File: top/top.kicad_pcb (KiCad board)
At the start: 2 copper layers, 28.3 x 40 mm, 26 parts, among them P1 CONN_10, P2 CONN_5, U1 IQS572, U4 ESD

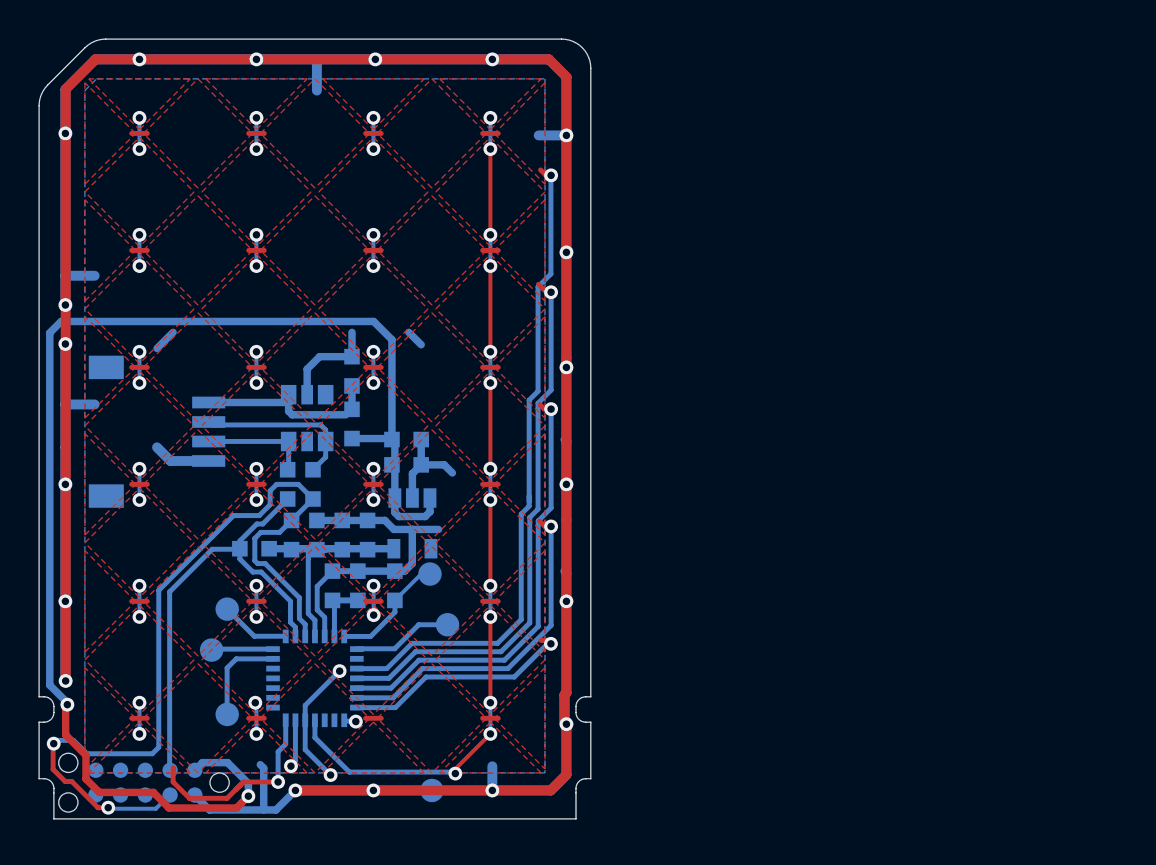
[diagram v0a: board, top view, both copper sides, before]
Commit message: Edit ESD GND ring.
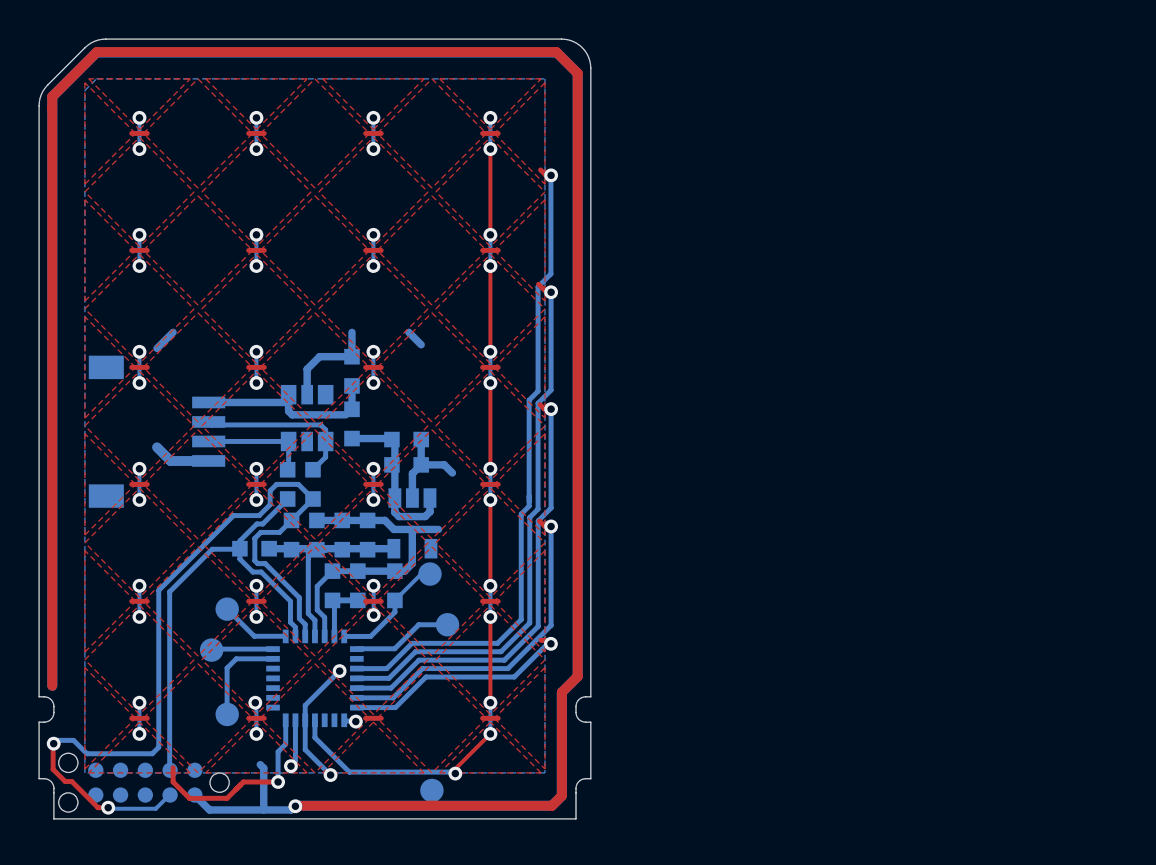
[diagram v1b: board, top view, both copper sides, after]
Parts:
- removed G***: LOGO, ugl:UHK_Logo_12x3.4_mm
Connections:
- P1 pad 2: +5V -> /VCC_BOTTOM
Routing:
- net +5V: track 68.7 -> 8.57 mm, vias 2 -> 0
- net GND: track 259.6 -> 259.0 mm, vias 19 -> 1

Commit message: New diamond pattern.
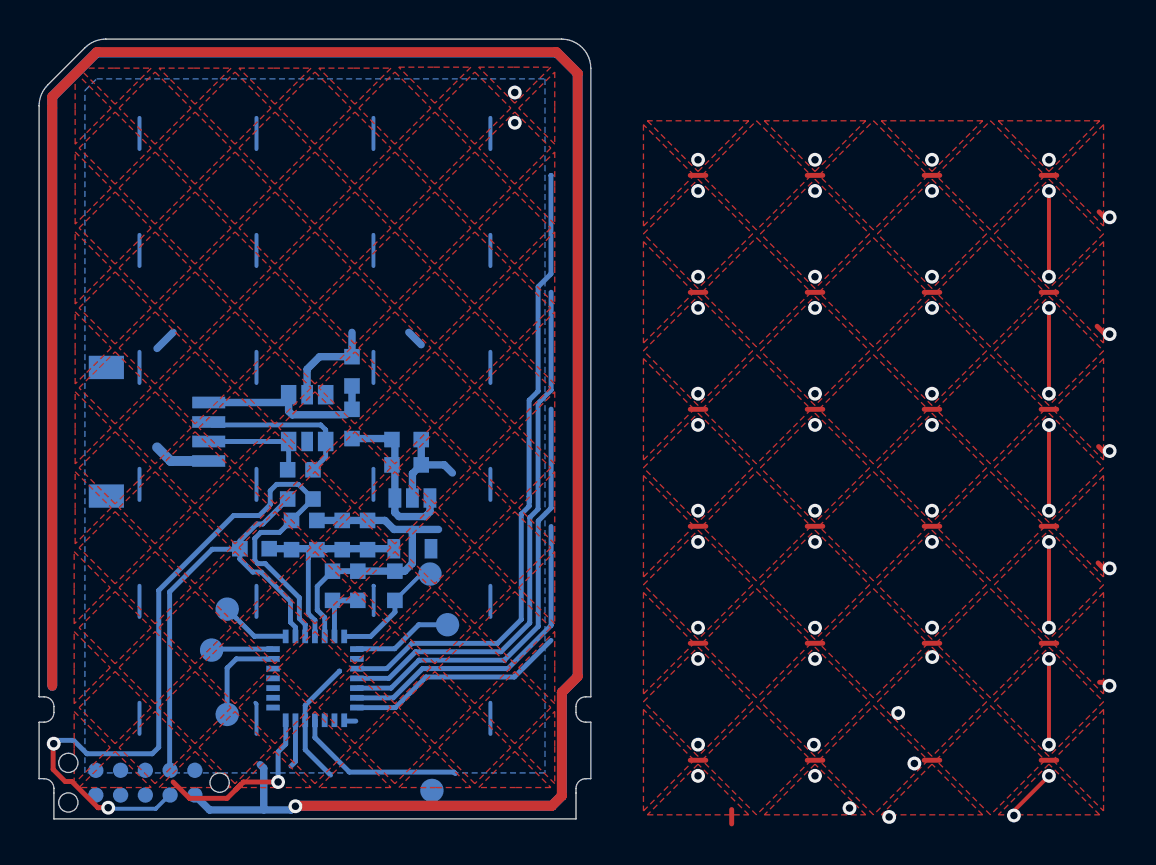
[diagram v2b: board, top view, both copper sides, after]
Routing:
- net (no net): vias 0 -> 2
- added copper zone on F.Cu, net (none)

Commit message: Wiring new pattern.
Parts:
- removed TP_NRST1: NRST, ugl:Test_Point
- removed TP_PGM1: PGM, ugl:Test_Point
- removed TP_RDY1: RDY, ugl:Test_Point
- moved TP_GND1 20.0 mm to (192.5, 151.5)
- moved C2 7.08 mm to (205.7, 135.0), turned to 90 degrees
- moved C8 5.32 mm to (206.9, 135.0), turned to 90 degrees
- moved VR1 5.08 mm to (209.8, 138.3)
- moved C7 5.00 mm to (202.6, 135.3)
- moved R1 4.65 mm to (208.6, 141.7), turned to 90 degrees
- moved C6 4.48 mm to (211.0, 141.7), turned to 90 degrees
- moved FB2 4.46 mm to (204.5, 135.0), turned to 90 degrees
- moved R2 4.24 mm to (205.7, 141.7), turned to 90 degrees
- moved TP_POUT1 3.47 mm to (202.9, 152.2)
- moved TP_TOUT1 2.79 mm to (201.9, 150.4)
- moved C12 2.61 mm to (209.8, 141.7), turned to 90 degrees
- moved C5 2.20 mm to (204.1, 145.3)
- moved U1 2.17 mm to (207.8, 150.7), turned to 315 degrees
- moved P2 1.90 mm to (196.2, 138.6)
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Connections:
- net Net-(U1-Pad22) renamed /TX4
- net Net-(U1-Pad23) renamed /TX5
- net Net-(U1-Pad24) renamed /TX6
- net Net-(U1-Pad25) renamed /TX7
- net Net-(U1-Pad26) renamed /TX8
- P1 pad 10: Net-(P1-Pad10) -> /PGM
- P1 pad 8: Net-(P1-Pad8) -> /RDY
- P1 pad 9: Net-(P1-Pad9) -> /NRST
- U1 pad 27: Net-(TP_PGM1-Pad1) -> /PGM
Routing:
- net (no net): track 0.00 -> 41.6 mm, vias 2 -> 0
- net /RX5: track 3.81 -> 40.5 mm, vias 1 -> 10
- net /RX4: track 15.2 -> 36.1 mm, vias 1 -> 11
- net /TX1: track 14.5 -> 34.5 mm, vias 12 -> 1
- net /RX3: track 20.5 -> 40.2 mm, vias 1 -> 10
- net /TX2: track 12.1 -> 31.4 mm, vias 13 -> 1
- net GND: track 259.0 -> 242.7 mm, vias 1 -> 7
- net /VCC_BOTTOM: track 9.56 -> 25.1 mm
- net /SCL: track 43.2 -> 28.4 mm
- net +3V3: track 11.6 -> 25.7 mm
- net /RX2: track 25.9 -> 34.5 mm, vias 1 -> 10
- net /TX3: track 20.1 -> 28.3 mm, vias 13 -> 1
- net /NRST: track 6.09 -> 0.00 mm
- net /RDY: track 5.14 -> 0.00 mm
- net /TX0: track 43.2 -> 38.3 mm, vias 13 -> 1
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- added copper zone on F.Cu, net /TX4
- added copper zone on F.Cu, net /TX5
- added copper zone on F.Cu, net /TX6
- added copper zone on F.Cu, net /TX7
- added copper zone on F.Cu, net /TX8
- added copper zone on In1.Cu, net GND
- removed copper zone on F.Cu, net (none)
- removed copper zone on B.Cu, net GND
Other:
- copper layers 2 -> 4

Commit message: First final modified board.
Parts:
- moved C1 17.7 mm to (193.3, 153.4), turned to 90 degrees
- moved TP_TOUT1 1.08 mm to (201.5, 151.4)
- moved C12 0.50 mm to (210.3, 141.7)
- moved C6 0.50 mm to (211.5, 141.7)
- moved TP_GND1 0.22 mm to (192.3, 151.4)
- moved C3 0.20 mm to (206.9, 145.5)
- moved C4 0.20 mm to (205.7, 145.5)
- moved C5 0.20 mm to (204.1, 145.5)
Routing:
- net (no net): track 41.6 -> 0.00 mm
- net /TX4: track 0.00 -> 30.1 mm, vias 0 -> 1
- net /NRST: track 0.00 -> 27.5 mm, vias 0 -> 2
- net /TX5: track 0.00 -> 26.4 mm, vias 0 -> 1
- net /RDY: track 0.00 -> 26.0 mm, vias 0 -> 2
- net /TX6: track 0.00 -> 25.0 mm, vias 0 -> 1
- net /RX0: track 34.5 -> 52.1 mm, vias 10 -> 11
- net /PGM: track 0.00 -> 13.8 mm, vias 0 -> 2
- net /RX1: track 34.5 -> 46.4 mm, vias 9 -> 11
- net /RX2: track 34.5 -> 43.4 mm, vias 10 -> 11
- net /TX8: track 3.44 -> 8.24 mm
- net /TX7: track 1.36 -> 6.16 mm
- net /TX1: track 34.5 -> 37.9 mm
- net /TX2: track 31.4 -> 34.8 mm
- net /TX3: track 28.3 -> 31.7 mm
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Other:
- rule via_min_size: 0.7112 -> 0.635

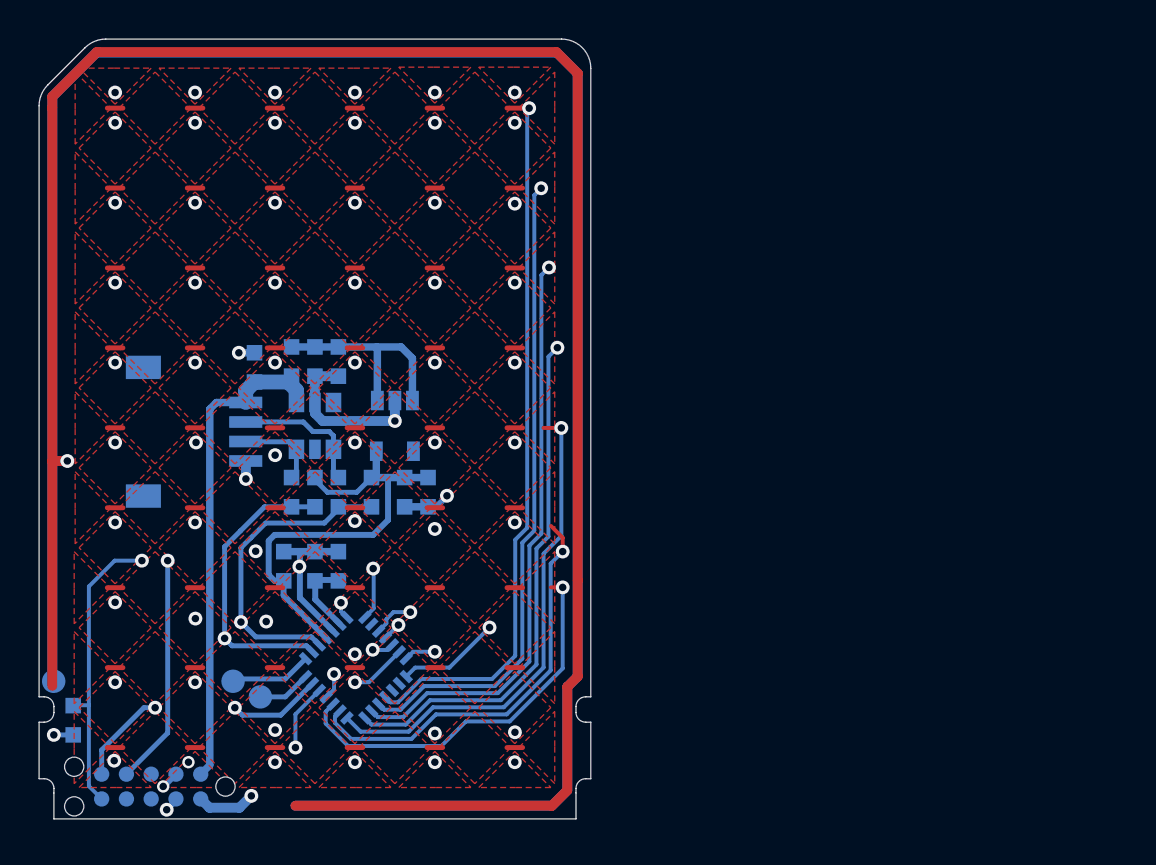
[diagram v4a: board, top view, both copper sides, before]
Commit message: Add a config header.
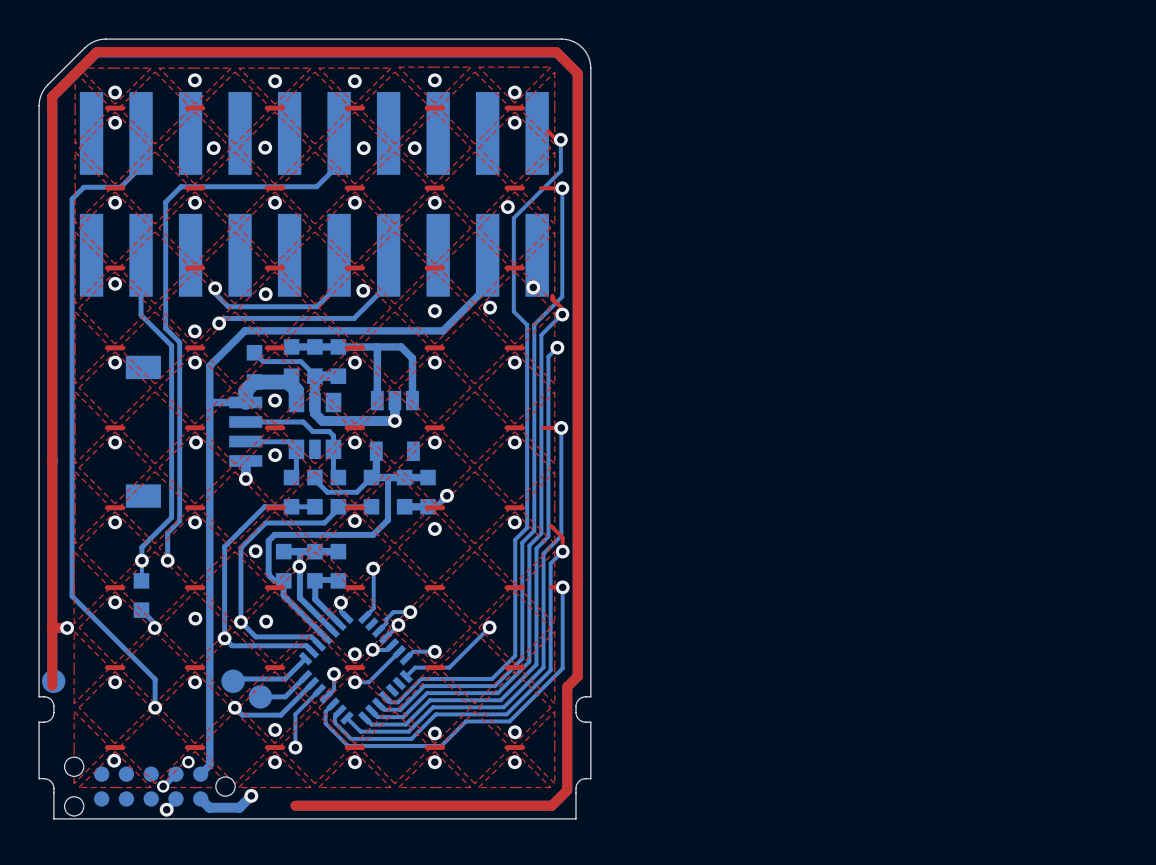
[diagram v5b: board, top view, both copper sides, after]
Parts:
- added P3: CONN_20, ugl:MC-254-20-00-ST-SMD, B.Cu at (205.9, 126.1)
- moved C1 7.29 mm to (196.8, 147.0)
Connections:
- P1 pad 10: /PGM -> Net-(P1-Pad10)
- P1 pad 8: /RDY -> Net-(P1-Pad8)
- P1 pad 9: /NRST -> Net-(P1-Pad9)
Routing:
- net /PGM: track 13.8 -> 42.7 mm
- net /SDA: track 25.5 -> 52.8 mm, vias 2 -> 3
- net /SCL: track 28.3 -> 55.1 mm, vias 2 -> 3
- net /VCC_BOTTOM: track 25.1 -> 44.7 mm
- net /RDY: track 26.0 -> 44.4 mm
- net /NRST: track 27.5 -> 30.3 mm
- net GND: track 245.7 -> 248.1 mm
- net /RX2: track 43.4 -> 45.1 mm
- net /RX4: track 36.1 -> 37.8 mm
- net /RX5: track 41.0 -> 42.6 mm
- net /RX1: track 46.4 -> 48.1 mm
- net /TX1: track 37.9 -> 39.4 mm
- net /RX3: track 37.4 -> 38.9 mm
- net /TX2: track 34.8 -> 33.9 mm
